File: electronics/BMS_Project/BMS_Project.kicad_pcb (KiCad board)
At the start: 2 copper layers, 0 parts

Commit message: Started PCB layout and adjusted schematic to suit the layout needs better
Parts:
- added C1: 10u?, Capacitor_SMD:C_0805_2012Metric, F.Cu at (149.8, 104.4)
- added F1: Fuse, Fuse:Fuse_1206_3216Metric, F.Cu at (160.5, 97.4)
- added J1: Conn_01x20_Pin, Connector_IDC:IDC-Header_2x10_P2.54mm_Vertical, F.Cu at (111.5, 85.3)
- added J2: Conn_01x01_Socket, Connector:Banana_Jack_1Pin, F.Cu at (190.0, 126.0)
- added J4: ESP32_power, TerminalBlock:TerminalBlock_bornier-2_P5.08mm, F.Cu at (193.7, 84.7)
- added J5: Display_power, TerminalBlock:TerminalBlock_bornier-2_P5.08mm, F.Cu at (193.6, 95.7)
- added J6: Conn_01x01_Socket, Connector:Banana_Jack_1Pin, F.Cu at (190.0, 111.0)
- added JP1: SolderJumper_2_Open, Jumper:SolderJumper-2_P1.3mm_Open_Pad1.0x1.5mm, F.Cu at (109.2, 52.1)
- added PAD1: Pin_17, BMS_lib:Prototyping_Pad_Data, F.Cu at (133.4, 92.0)
- added PAD2: Pin_18, BMS_lib:Prototyping_Pad_Data, F.Cu at (137.2, 92.0)
- added Q1: Q_PMOS_GSD, Package_TO_SOT_SMD:SOT-23, F.Cu at (158.5, 121.0)
- added R1: 100k, Resistor_SMD:R_0805_2012Metric, F.Cu at (133.5, 44.2)
- added R10: 100k, Resistor_SMD:R_0805_2012Metric, F.Cu at (133.5, 46.7)
- added R11: 100k, Resistor_SMD:R_0805_2012Metric, F.Cu at (118.6, 47.8)
- added R12: 100k, Resistor_SMD:R_0805_2012Metric, F.Cu at (120.1, 44.1)
- added R13: 100k, Resistor_SMD:R_0805_2012Metric, F.Cu at (133.6, 67.6)
- added R14: 100k, Resistor_SMD:R_0805_2012Metric, F.Cu at (133.6, 63.8)
- added R15: 100k, Resistor_SMD:R_0805_2012Metric, F.Cu at (119.7, 64.8)
- added R16: 100k, Resistor_SMD:R_0805_2012Metric, F.Cu at (119.7, 61.0)
- added R17: 4.7k, Resistor_SMD:R_0805_2012Metric, F.Cu at (149.8, 100.9)
- added R2: 100k, Resistor_SMD:R_0805_2012Metric, F.Cu at (120.1, 41.6)
- added R29: 100k, Resistor_SMD:R_0805_2012Metric, F.Cu at (148.1, 79.0)
- added R3: 100k, Resistor_SMD:R_0805_2012Metric, F.Cu at (133.6, 61.9)
- added R30: 100k, Resistor_SMD:R_0805_2012Metric, F.Cu at (148.1, 81.5)
- added R31: 100k, Resistor_SMD:R_0805_2012Metric, F.Cu at (148.1, 84.1)
- added R32: 100k, Resistor_SMD:R_0805_2012Metric, F.Cu at (148.1, 86.6)
- added R4: 100k, Resistor_SMD:R_0805_2012Metric, F.Cu at (120.5, 58.3)
- added R5: 100k, Resistor_SMD:R_0805_2012Metric, F.Cu at (126.9, 51.9)
- added R6: 100k, Resistor_SMD:R_0805_2012Metric, F.Cu at (120.5, 47.8)
- added R7: 100k, Resistor_SMD:R_0805_2012Metric, F.Cu at (133.6, 65.7)
- added R8: 100k, Resistor_SMD:R_0805_2012Metric, F.Cu at (119.7, 62.9)
- added R9: 100k, Resistor_SMD:R_0805_2012Metric, F.Cu at (133.5, 49.2)
- added SW1: SW_Push, Button_Switch_SMD:SW_Push_1P1T_NO_6x6mm_H9.5mm, F.Cu at (113.3, 114.0)
- added SW2: SW_SPDT, Button_Switch_THT:SW_Slide_1P2T_CK_OS102011MS2Q, F.Cu at (173.4, 84.5)
- added SW3: SW_Push, Button_Switch_SMD:SW_Push_1P1T_NO_6x6mm_H9.5mm, F.Cu at (123.8, 114.0)
- added SW4: SW_Push, Button_Switch_SMD:SW_Push_1P1T_NO_6x6mm_H9.5mm, F.Cu at (134.2, 114.0)
- added SW5: SW_Push, Button_Switch_SMD:SW_Push_1P1T_NO_6x6mm_H9.5mm, F.Cu at (144.5, 114.0)
- added U1: LM358, Package_DIP:DIP-8_W7.62mm, F.Cu at (123.0, 41.6)
- added U2: LM358, Package_DIP:DIP-8_W7.62mm, F.Cu at (122.9, 57.8)
- added U3: Buck, BMS_lib:Buck_LM2596, F.Cu at (160.6, 132.1)
- added U4: ~, BMS_lib:CAN_Board, F.Cu at (171.9, 75.8)
- added XA1: Arduino_Mega2560_Shield, PCM_arduino-library:Arduino_Mega2560_Shield, B.Cu at (154.8, 28.2)
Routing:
- net GND: track 0.00 -> 156.9 mm
- net +5V: track 0.00 -> 118.4 mm
- net /CAN_CS: track 0.00 -> 81.6 mm
- net /CAN_SO: track 0.00 -> 81.4 mm
- net /CAN_SI: track 0.00 -> 75.4 mm
- net /CAN_SCK: track 0.00 -> 70.9 mm
- net /bat03: track 0.00 -> 52.7 mm
- net /bat_main_switch: track 0.00 -> 49.1 mm
- net /balancing_ctrl_4: track 0.00 -> 44.6 mm
- net /balancing_ctrl_2: track 0.00 -> 43.5 mm
- net /balancing_ctrl_3: track 0.00 -> 41.0 mm
- net /balancing_ctrl_1: track 0.00 -> 39.9 mm
- net /bat04: track 0.00 -> 39.9 mm
- net Net-(J6-Pin_1): track 0.00 -> 33.4 mm
- net /temp_sensor04: track 0.00 -> 32.5 mm
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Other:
- board outline added: 100 x 100 mm

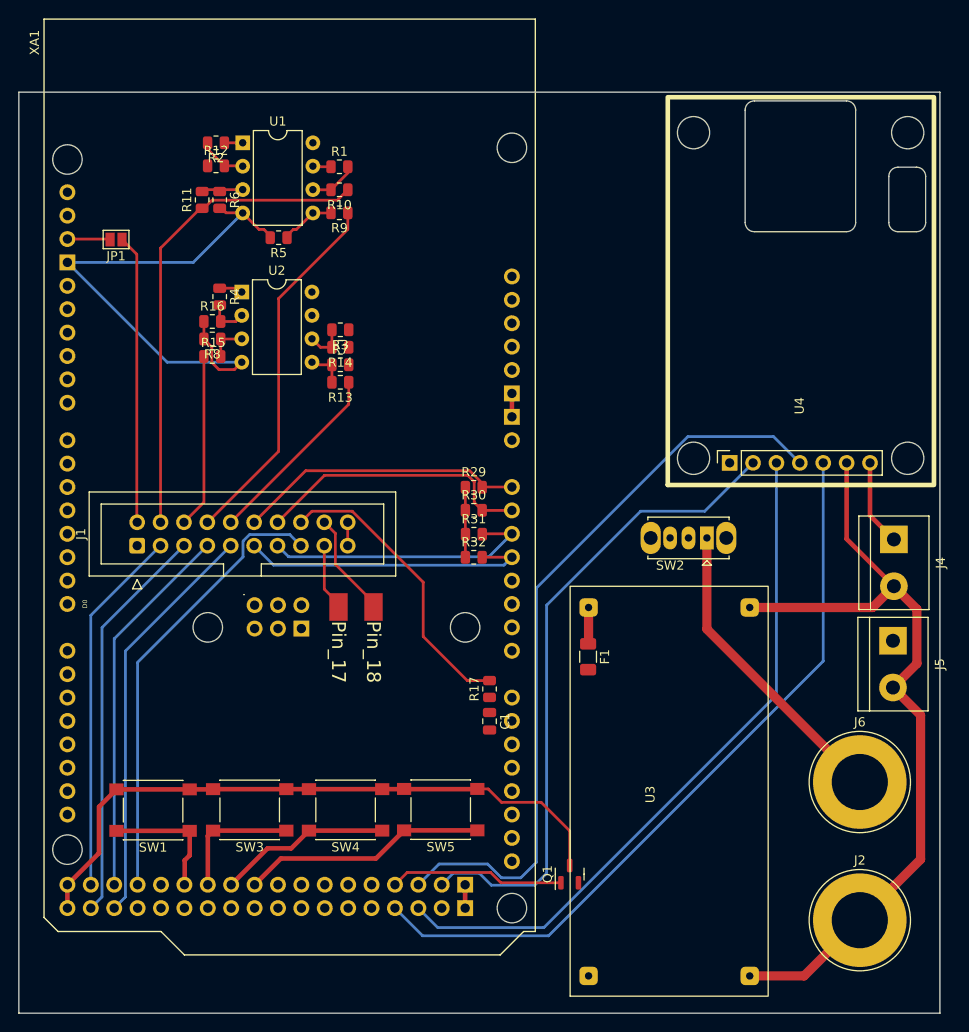
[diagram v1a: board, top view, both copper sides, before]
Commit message: Finished layout of main board and finalized lyout of cell board (added names & THI logo), changed pinout of tray plug
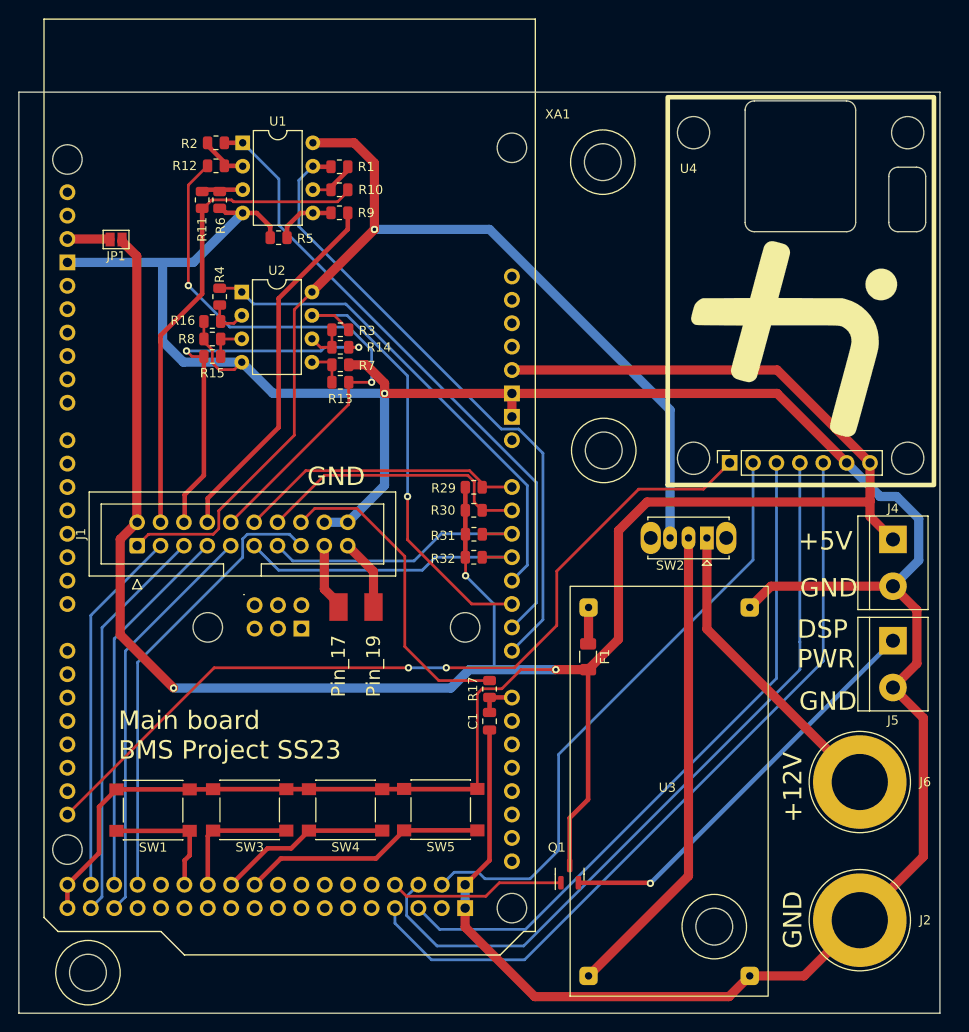
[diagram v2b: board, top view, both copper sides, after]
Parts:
- added G***: LOGO, BMS_lib:thi_logo_large, F.Cu at (182.9, 62.9)
- added G***: LOGO, BMS_lib:thi_logo_large, B.Cu at (169.0, 109.9)
- added M1: Prototyping_Wood_Hole, BMS_lib:Prototyping_Wood_Hole, F.Cu at (162.1, 43.7)
- added M2: Prototyping_Wood_Hole, BMS_lib:Prototyping_Wood_Hole, F.Cu at (106.2, 131.7)
- added M3: Prototyping_Wood_Hole, BMS_lib:Prototyping_Wood_Hole, F.Cu at (174.2, 126.7)
- added M4: Prototyping_Wood_Hole, BMS_lib:Prototyping_Wood_Hole, F.Cu at (162.2, 75.0)
- PAD2: value Pin_18 -> Pin_19
- moved J4 0.10 mm to (193.6, 84.7)
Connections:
- J1 pad 18: Net-(J1-Pin_18) -> GND
- J1 pad 19: GND -> Net-(J1-Pin_19)
- PAD2 pad 1: Net-(J1-Pin_18) -> Net-(J1-Pin_19)
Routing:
- net +5V: track 118.4 -> 313.4 mm, vias 0 -> 3
- net GND: track 156.9 -> 302.3 mm, vias 0 -> 1
- net +BATT: track 0.00 -> 118.0 mm, vias 0 -> 1
- net /CAN_INT: track 0.00 -> 91.2 mm, vias 0 -> 2
- net /Arduino/cell_3_V: track 1.99 -> 68.9 mm
- net /Arduino/cell_4_V: track 1.99 -> 68.7 mm
- net Net-(SW2-B): track 0.00 -> 52.0 mm
- net /Arduino/cell_1_V: track 2.57 -> 53.3 mm
- net /Arduino/cell_2_V: track 0.00 -> 49.8 mm, vias 0 -> 1
- net Net-(J5-Pin_1): track 0.00 -> 45.1 mm, vias 0 -> 1
- net /bat02: track 20.5 -> 63.2 mm, vias 0 -> 2
- net /bat01: track 18.9 -> 41.0 mm, vias 0 -> 2
- net Net-(J1-Pin_18): track 11.4 -> 0.00 mm
- net Net-(J1-Pin_19): track 0.00 -> 7.82 mm
- net /CAN_SCK: track 70.9 -> 65.6 mm
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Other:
- board text added: "+12V"
- board text added: "+5V"
- board text added: "DSP PWR"
- board text added: "GND"
- board text added: "Main board BMS Project SS23"
- board text added: "Tjorven Hillmann Wilken Hemme Henry Pasch Michael Witti Jonathan Böke Fabian Mast Gina-Madeleine Haase A. Furkan Can Ramón Fürst"

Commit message: changed the value of one capacitor
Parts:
- C1: value 10u? -> 10u
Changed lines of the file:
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@@
         (effects (font (size 1 1) (thickness 0.15)))
     )
-    (fp_text value "10u?" (at 0 1.68 90) (layer "F.Fab")
+    (fp_text value "10u" (at 0 1.68 90) (layer "F.Fab")
         (effects (font (size 1 1) (thickness 0.15)))
     )
@@
     (fp_arc (start 94.488 -0.254) (mid 96.52 -0.914237) (end 98.552 -0.254)
       (stroke (width 0.15) (type solid)) (layer "F.CrtYd"))
-    (fp_arc (start 99.314 0.508) (mid 99.650926 1.077973) (end 99.8728 1.7018)
+    (fp_arc (start 99.314 0.508) (mid 99.650928 1.077972) (end 99.8728 1.7018)
       (stroke (width 0.15) (type solid)) (layer "F.CrtYd"))
     (fp_circle (center 13.97 2.54) (end 17.17 2.54)

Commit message: exported PCB's as gerber files
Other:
- board text added: "JLCJLCJLCJLC"
